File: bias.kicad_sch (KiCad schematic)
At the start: 31 parts, among them Q1901 DPLS350E, Q1902 DNLS350E, Q1903 DPLS350E, Q1904 DPLS350E, Q1905 DNLS350E, Q1906 DNLS350E, Q1907 TIP41C, Q1908 TIP42C

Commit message: edit trimmer adjustment style to sideways
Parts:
- RV1901: footprint pss:Potentiometer_Bourns_PVG5A -> pss:Potentiometer_Bourns_PVG5H; MPN PVG5A102C03B00 -> PVG5H102C03R00; VPN 81-PVG5A102C03B00 -> 81-PVG5H102C03R00
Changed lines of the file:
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@@
 		(title "Power Supply Sink")
 		(date "2024-12-07")
-		(rev "0.13.3")
+		(rev "0.13.4")
 		(company "Open Battery Tester")
 		(comment 1 "Bias Stage")
@@
 			)
 		)
-		(property "Footprint" "pss:Potentiometer_Bourns_PVG5A"
+		(property "Footprint" "pss:Potentiometer_Bourns_PVG5H"
 			(at 60.96 107.95 0)
 			(effects
@@
 			)
 		)
-		(property "MPN" "PVG5A102C03B00"
+		(property "MPN" "PVG5H102C03R00"
 			(at 60.96 107.95 0)
 			(effects
@@
 			)
 		)
-		(property "VPN" "81-PVG5A102C03B00"
+		(property "VPN" "81-PVG5H102C03R00"
 			(at 60.96 107.95 0)
 			(effects

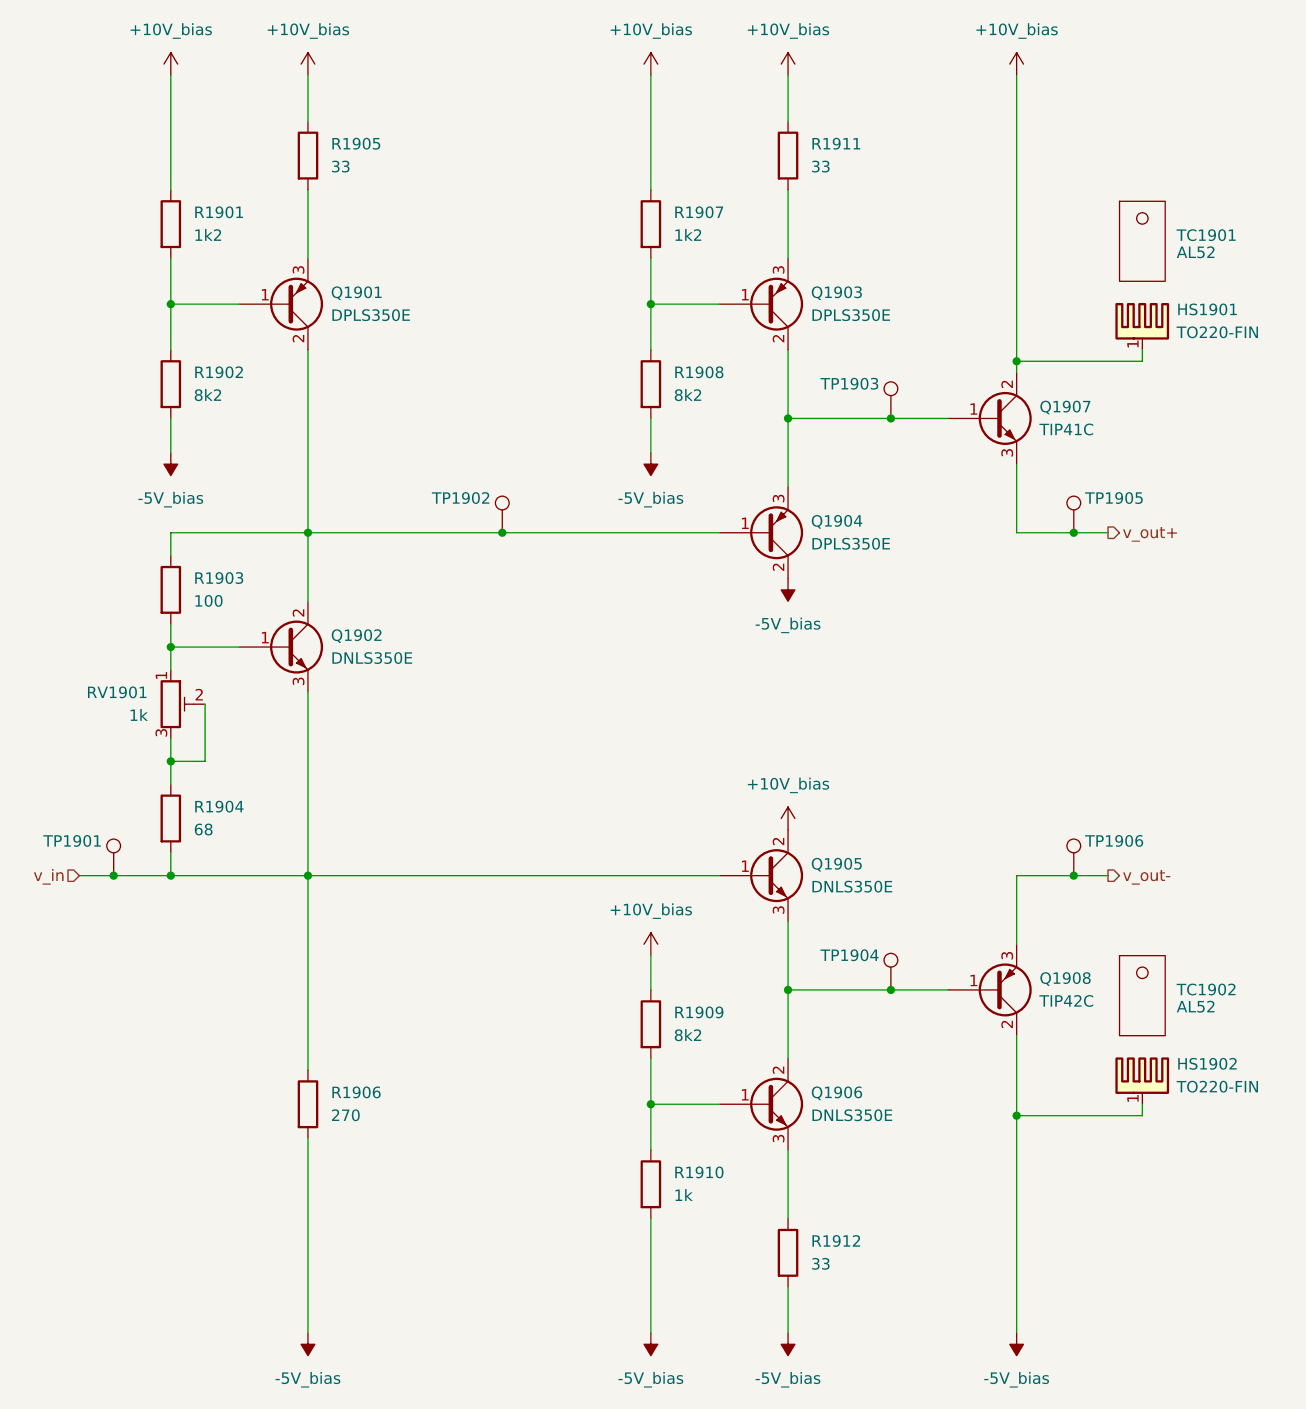
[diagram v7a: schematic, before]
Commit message: fix bias heatsink unconnected electrical connection
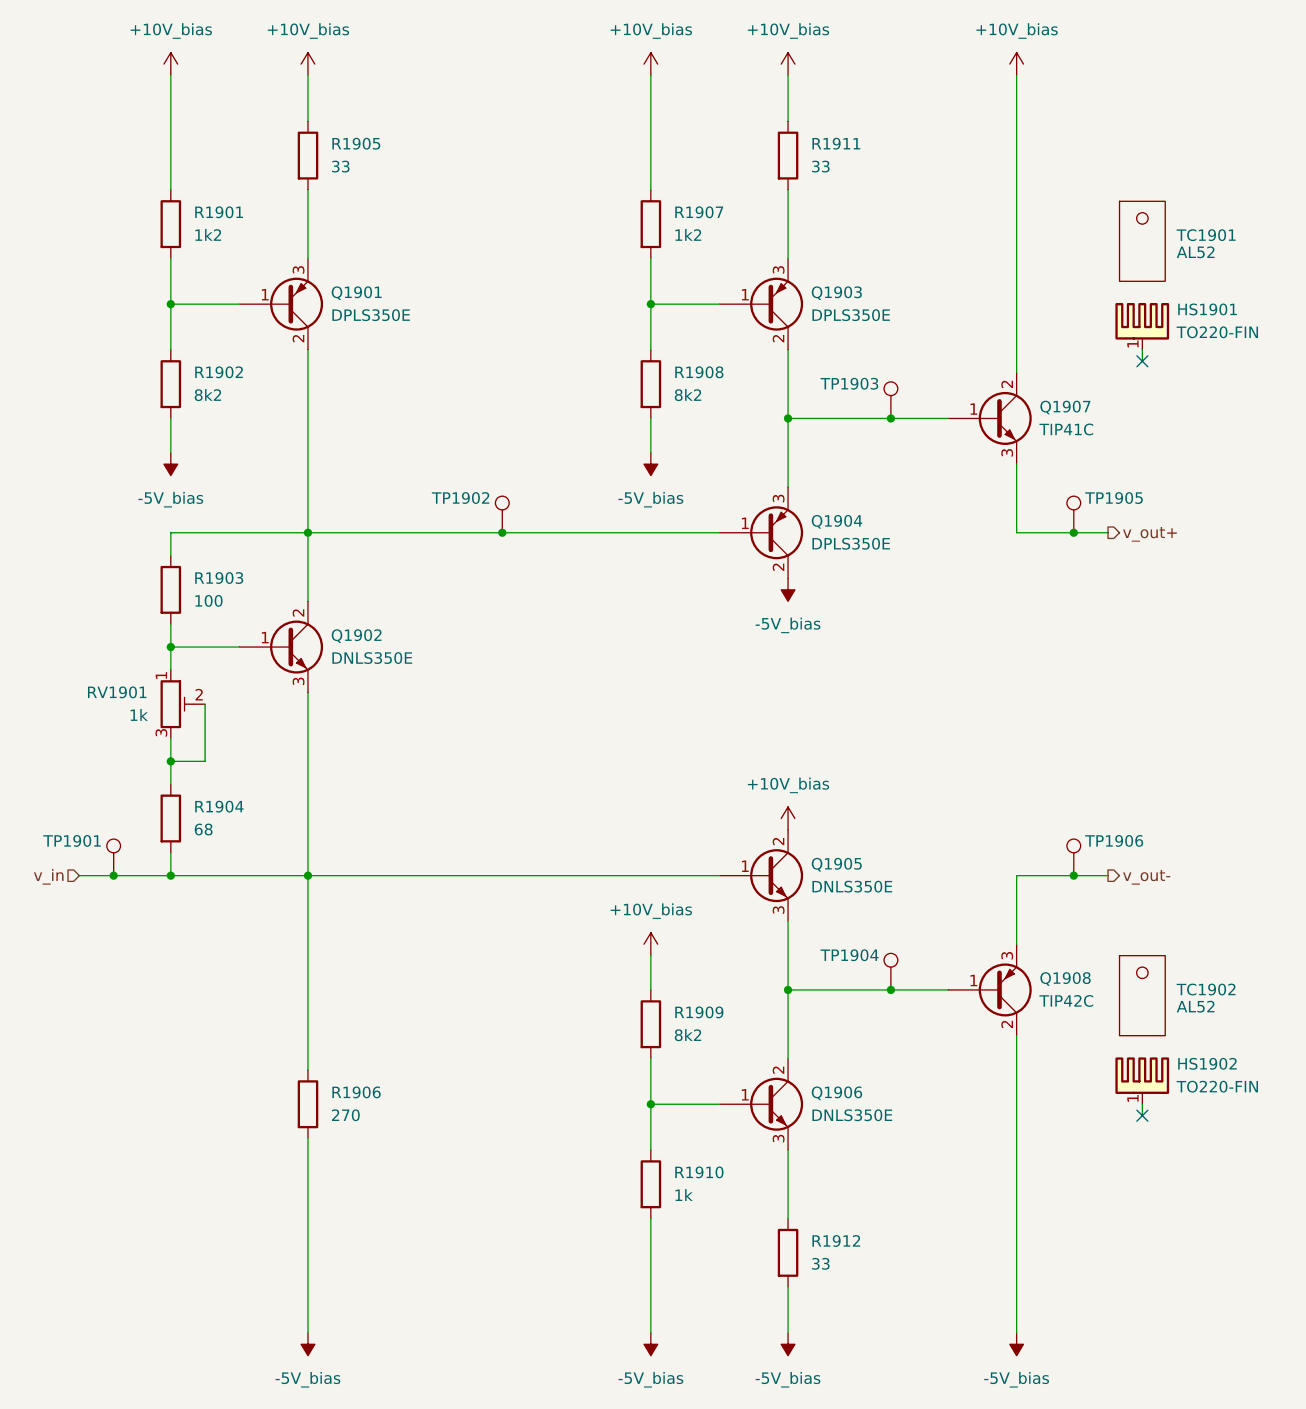
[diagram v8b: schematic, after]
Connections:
- net +10V_bias: no longer HS1901.1
- net -5V_bias: no longer HS1902.1
- no-connect marks 0 -> 2
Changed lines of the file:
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@@
 		(title "Power Supply Sink")
 		(date "2024-12-10")
-		(rev "0.14.0")
+		(rev "0.14.2")
 		(company "Open Battery Tester")
 		(comment 1 "Bias Stage")
@@
 	)
 	(junction
-		(at 154.94 153.67)
-		(diameter 0)
-		(color 0 0 0 0)
-	)
-	(junction
 		(at 60.96 127)
 		(diameter 0)
@@
 	)
 	(junction
-		(at 154.94 69.85)
-		(diameter 0)
-		(color 0 0 0 0)
-	)
-	(junction
 		(at 129.54 76.2)
 		(diameter 0)
@@
 		(color 0 0 0 0)
 	)
+	(no_connect
+		(at 168.91 69.85)
+	)
+	(no_connect
+		(at 168.91 153.67)
+	)
 	(wire
 		(pts
@@
 	(wire
 		(pts
-			(xy 154.94 144.78) (xy 154.94 153.67)
+			(xy 154.94 144.78) (xy 154.94 177.8)
 		)
 		(stroke
@@
 	(wire
 		(pts
-			(xy 168.91 153.67) (xy 154.94 153.67)
-		)
-		(stroke
-			(width 0)
-			(type default)
-		)
-	)
-	(wire
-		(pts
 			(xy 161.29 127) (xy 154.94 127)
 		)
@@
 	(wire
 		(pts
-			(xy 154.94 69.85) (xy 154.94 71.12)
+			(xy 154.94 38.1) (xy 154.94 71.12)
 		)
 		(stroke
@@
 	(wire
 		(pts
-			(xy 154.94 69.85) (xy 168.91 69.85)
-		)
-		(stroke
-			(width 0)
-			(type default)
-		)
-	)
-	(wire
-		(pts
-			(xy 154.94 38.1) (xy 154.94 69.85)
-		)
-		(stroke
-			(width 0)
-			(type default)
-		)
-	)
-	(wire
-		(pts
 			(xy 60.96 101.6) (xy 68.58 101.6)
 		)
 		(stroke
-			(width 0)
-			(type default)
-		)
-	)
-	(wire
-		(pts
-			(xy 154.94 153.67) (xy 154.94 177.8)
-		)
-		(stroke
